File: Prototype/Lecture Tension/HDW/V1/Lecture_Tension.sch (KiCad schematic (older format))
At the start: 40 parts

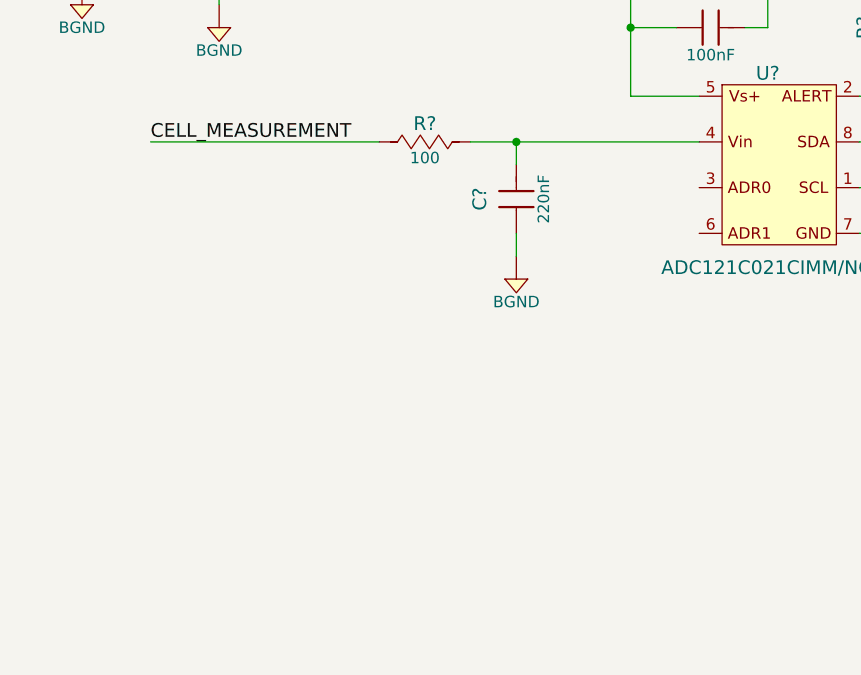
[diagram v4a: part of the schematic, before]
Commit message: add ADR0-1 header
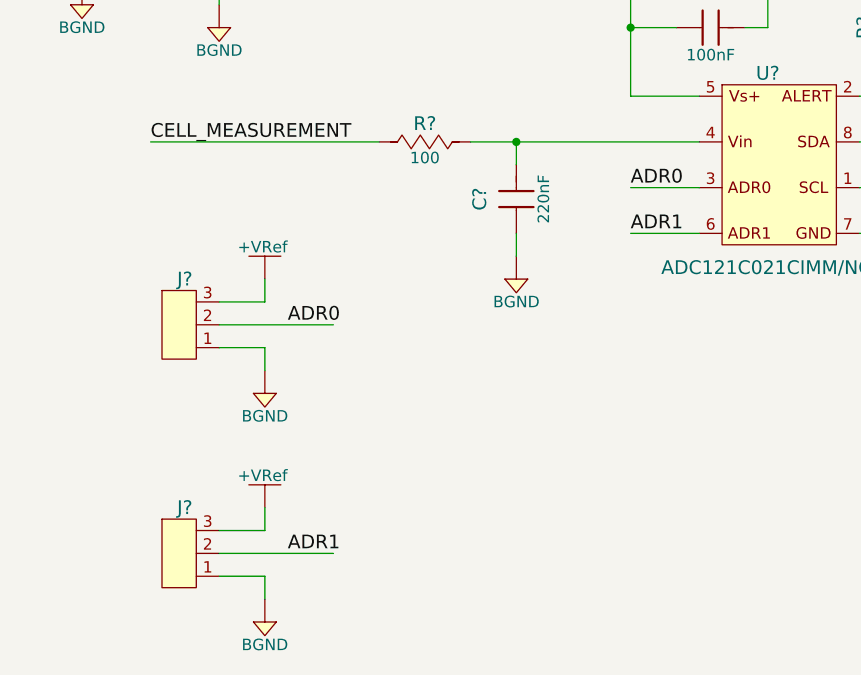
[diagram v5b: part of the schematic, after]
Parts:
- added J? (x2): Header_Male_Pin_2.54mm_1X3_,_Unshrouded, Connectors:Headers_2.54mm_1X3, symbol Header_Male_Pin_2.54mm_1X3_,_Unshrouded
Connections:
- net +VRef: now also J?.3, J?.3
- net BGND: now also J?.1, J?.1
- net ADR0: now reaches U?.3 (ADR0)
- net ADR0: now also J?.2
- net ADR1: now reaches U?.6 (ADR1)
- net ADR1: now also J?.2
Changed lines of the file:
@@
 	0    -1   -1   0
 $EndComp
+$Comp
+L Header_Male_Pin_2.54mm_1X3_,_Unshrouded J?
+U 1 1 591CA9FD
+P 3300 6500
+F 0 "J?" H 3250 6800 60  0000 C CNN
+F 1 "Header_Male_Pin_2.54mm_1X3_,_Unshrouded" H 3300 6180 50  0001 C CNN
+F 2 "Connectors:Headers_2.54mm_1X3" H 3300 5590 30  0001 C CNN
+F 3 "D" H 3300 5540 30  0001 C CNN
+F 4 "Ebay" H 3300 5990 60  0001 C CNN "Supplier"
+F 5 "Pin Male Single Row Pin Header Strip" H 3300 6090 60  0001 C CNN "Supplier Part Number"
+F 6 "Manufacturer" H 3300 5890 60  0001 C CNN "Manufacturer"
+F 7 "Manufacturer Part Number" H 3300 5790 60  0001 C CNN "Manufacturer Part Number"
+F 8 "Pin Male Single Row Pin Header Strip" H 3300 5690 60  0001 C CNN "Description"
+	1    3300 6500
+	1    0    0    -1
+$EndComp
+$Comp
+L +VRef #PWR?
+U 1 1 591CAC97
+P 3600 6200
+F 0 "#PWR?" H 3600 6050 50  0001 C CNN
+F 1 "+VRef" H 3590 6340 50  0000 C CNN
+F 2 "" H 3600 6200 60  0000 C CNN
+F 3 "" H 3600 6200 60  0000 C CNN
+	1    3600 6200
+	1    0    0    -1
+$EndComp
+Wire Wire Line
+	3600 6200 3600 6300
+Wire Wire Line
+	3600 6300 3400 6300
+$Comp
+L BGND #PWR?
+U 1 1 591CAE09
+P 3600 6700
+F 0 "#PWR?" H 3600 6530 50  0001 C CNN
+F 1 "BGND" H 3600 6600 50  0000 C CNN
+F 2 "" H 3600 6800 60  0000 C CNN
+F 3 "" H 3580 6610 60  0000 C CNN
+	1    3600 6700
+	1    0    0    -1
+$EndComp
+Wire Wire Line
+	3400 6500 3600 6500
+Wire Wire Line
+	3600 6500 3600 6600
+Wire Wire Line
+	3400 6400 3900 6400
+Text Label 3700 6400 0    60   ~ 0
+ADR0
+$Comp
+L Header_Male_Pin_2.54mm_1X3_,_Unshrouded J?
+U 1 1 591CB232
+P 3300 7500
+F 0 "J?" H 3250 7800 60  0000 C CNN
+F 1 "Header_Male_Pin_2.54mm_1X3_,_Unshrouded" H 3300 7180 50  0001 C CNN
+F 2 "Connectors:Headers_2.54mm_1X3" H 3300 6590 30  0001 C CNN
+F 3 "D" H 3300 6540 30  0001 C CNN
+F 4 "Ebay" H 3300 6990 60  0001 C CNN "Supplier"
+F 5 "Pin Male Single Row Pin Header Strip" H 3300 7090 60  0001 C CNN "Supplier Part Number"
+F 6 "Manufacturer" H 3300 6890 60  0001 C CNN "Manufacturer"
+F 7 "Manufacturer Part Number" H 3300 6790 60  0001 C CNN "Manufacturer Part Number"
+F 8 "Pin Male Single Row Pin Header Strip" H 3300 6690 60  0001 C CNN "Description"
+	1    3300 7500
+	1    0    0    -1
+$EndComp
+$Comp
+L +VRef #PWR?
+U 1 1 591CB238
+P 3600 7200
+F 0 "#PWR?" H 3600 7050 50  0001 C CNN
+F 1 "+VRef" H 3590 7340 50  0000 C CNN
+F 2 "" H 3600 7200 60  0000 C CNN
+F 3 "" H 3600 7200 60  0000 C CNN
+	1    3600 7200
+	1    0    0    -1
+$EndComp
+Wire Wire Line
+	3600 7200 3600 7300
+Wire Wire Line
+	3600 7300 3400 7300
+$Comp
+L BGND #PWR?
+U 1 1 591CB240
+P 3600 7700
+F 0 "#PWR?" H 3600 7530 50  0001 C CNN
+F 1 "BGND" H 3600 7600 50  0000 C CNN
+F 2 "" H 3600 7800 60  0000 C CNN
+F 3 "" H 3580 7610 60  0000 C CNN
+	1    3600 7700
+	1    0    0    -1
+$EndComp
+Wire Wire Line
+	3400 7500 3600 7500
+Wire Wire Line
+	3600 7500 3600 7600
+Wire Wire Line
+	3400 7400 3900 7400
+Text Label 3700 7400 0    60   ~ 0
+ADR1
+Wire Wire Line
+	5200 5800 5500 5800
+Text Label 5200 5800 0    60   ~ 0
+ADR0
+Wire Wire Line
+	5200 6000 5500 6000
+Text Label 5200 6000 0    60   ~ 0
+ADR1
 $EndSCHEMATC
